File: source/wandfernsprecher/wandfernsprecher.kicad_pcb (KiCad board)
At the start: 2 copper layers, 132.5 x 82 mm, 65 parts, among them J1 Hörer, J2 USB_C_Receptacle_USB2.0, J3 Conn_01x02, Q1 AO3400A, Q10 AO3401A, Q11 AO3400A, Q2 2N5551, Q3 2N5551, Q4 2N5551, Q5 2N5401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

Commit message: completed layout
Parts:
- removed C18: 100n, Capacitor_SMD:C_0603_1608Metric
- removed J2: USB_C_Receptacle_USB2.0, Connector_USB:USB_C_Receptacle_HRO_TYPE-C-31-M-12
- removed R24: 10k, Resistor_SMD:R_0603_1608Metric
- removed R25, R27: 5k1, Resistor_SMD:R_0603_1608Metric
- added BT1: Battery_Cell, Connector_JST:JST_PH_B2B-PH-K_1x02_P2.00mm_Vertical, F.Cu at (90.8, 84.5)
- added C10: 100nF, Capacitor_SMD:C_0603_1608Metric, F.Cu at (84.5, 126.2)
- added C19: 10µF, Capacitor_SMD:C_0603_1608Metric, F.Cu at (86.8, 142.2)
- added C20: 1µF, Capacitor_SMD:C_0603_1608Metric, F.Cu at (86.5, 138.5)
- added C6: 1µF, Capacitor_SMD:C_0603_1608Metric, F.Cu at (95.8, 98.1)
- added C7: 1µF, Capacitor_SMD:C_0603_1608Metric, F.Cu at (93.8, 92.3)
- added C8: 10µF, Capacitor_SMD:C_0603_1608Metric, F.Cu at (82.0, 126.2)
- added C9: 10nF, Capacitor_SMD:C_0603_1608Metric, F.Cu at (79.5, 121.8)
- added D2: GRN, LED_SMD:LED_0805_2012Metric, F.Cu at (81.8, 82.5)
- added D3: YEL, LED_SMD:LED_0805_2012Metric, F.Cu at (84.0, 82.5)
- added D4: 5,1V, Diode_SMD:D_SOD-123, F.Cu at (102.5, 81.0)
- added JP1: SolderJumper_2_Open, Jumper:SolderJumper-2_P1.3mm_Open_RoundedPad1.0x1.5mm, F.Cu at (90.8, 99.2)
- added JP2: SolderJumper_2_Open, Jumper:SolderJumper-2_P1.3mm_Open_RoundedPad1.0x1.5mm, F.Cu at (88.2, 99.2)
- added R28: 1k6, Resistor_SMD:R_0603_1608Metric, F.Cu at (90.2, 96.0)
- added R29: 820, Resistor_SMD:R_0603_1608Metric, F.Cu at (88.8, 96.0)
- added R30: 1k, Resistor_SMD:R_0603_1608Metric, F.Cu at (97.2, 87.8)
- added R31: 10k, Resistor_SMD:R_0603_1608Metric, F.Cu at (95.8, 87.8)
- added R32: 1k6, Resistor_SMD:R_0603_1608Metric, F.Cu at (101.5, 95.0)
- added R33: 1k6, Resistor_SMD:R_0603_1608Metric, F.Cu at (101.5, 93.2)
- added SW3: SW_SPST, Connector_JST:JST_PH_B2B-PH-K_1x02_P2.00mm_Vertical, F.Cu at (100.8, 75.0)
- added U8: TPS73633DBV, Package_TO_SOT_SMD:SOT-23-5, F.Cu at (83.2, 122.8)
- C1, C11, C16, C2, C3, C4, C5: value 100n -> 100nF
- C13, C15: value 1µ -> 1µF
- J1, NS1, SW2: footprint FeWAp:CONN_01x04_vertical -> FeWAp:CONN_01x04_vertical_mod
- J3: value Conn_01x02 -> Conn_01x04; footprint Connector_JST:JST_PH_B2B-PH-K_1x02_P2.00mm_Vertical -> Connector_PinHeader_2.54mm:PinHeader_1x04_P2.54mm_Vertical
- L1: footprint FeWAp:CONN_01x02_vertical -> FeWAp:CONN_01x02_vertical_mod
- U2: footprint Espressif:ESP32-C3-WROOM-02 -> RF_Module:ESP32-C3-WROOM-02
- moved R17 240.2 mm to (124.8, 131.2), turned to -90 degrees
- moved R18 237.3 mm to (124.8, 128.0), turned to -90 degrees
- moved D1 236.4 mm to (121.0, 136.5), turned to 180 degrees
- moved U4 227.8 mm to (115.2, 125.1), turned to -90 degrees
- moved R16 227.8 mm to (112.8, 124.2), turned to -90 degrees
- moved R8 225.0 mm to (100.8, 132.5), turned to 0 degrees
- moved Q1 224.0 mm to (100.8, 135.2)
- moved R10 223.6 mm to (101.8, 138.8), turned to -90 degrees
- moved C13 221.9 mm to (109.5, 124.0), turned to 180 degrees
- moved Q8 221.1 mm to (100.8, 142.2), turned to -90 degrees
- moved R9 220.8 mm to (99.8, 138.8), turned to -90 degrees
- moved C14 217.7 mm to (125.0, 144.2), turned to 180 degrees
- moved L2 217.5 mm to (107.0, 143.0), turned to 0 degrees
- moved C12 216.2 mm to (108.0, 133.6), turned to 90 degrees
- moved Q2 190.9 mm to (131.2, 136.2)
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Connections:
- net Net-(C13-Pad1) renamed /Bells/HV_{C}'
- net Net-(J1-MIC+) renamed /S+
- net Net-(J1-MIC-) renamed /S-
- net Net-(J1-SPK+) renamed /M+
- net Net-(J1-SPK-) renamed /M-
- net Net-(Q1-D) renamed /Bells/~{HV_EN}
- net Net-(Q8-D) renamed /Bells/HV-IN
- net Net-(U4-FB) renamed /Bells/HV-FB
- net Net-(U4-V_{C}) renamed /Bells/HV-C
- C15 pad 1: Net-(Q4-E) -> Net-(Q6-E)
- J3 pad 1: +BATT -> GND
- J3 pad 2: GND -> /plug.D+
- L1 pad 1: Net-(C15-Pad2) -> Net-(Q4-E)
- L1 pad 2: Net-(Q6-E) -> Net-(C15-Pad2)
- U2 pad 10: BELL_B -> nsa
- U2 pad 3: nsa -> BELL_B
- U2 pad 4: nsi -> BELL_A
- U2 pad 6: BELL_A -> nsi
- U3 pad 1: unconnected-(U3-IN-Pad1) -> VBUS
- U3 pad 10: unconnected-(U3-OUT-Pad10) -> +BATT
- U3 pad 11: Net-(U3-VSS-Pad11) -> GND
- U3 pad 2: unconnected-(U3-ISET-Pad2) -> /Power Supply/ISET
- U3 pad 3: Net-(U3-VSS-Pad11) -> GND
- U3 pad 5: unconnected-(U3-~{PG}-Pad5) -> /Power Supply/BQ-~{PG}
- U3 pad 7: unconnected-(U3-ISET2-Pad7) -> /Power Supply/ISET2
- U3 pad 8: unconnected-(U3-~{CHG}-Pad8) -> /Power Supply/BQ-~{CHG}
- U3 pad 9: unconnected-(U3-TS-Pad9) -> /Power Supply/TS
- U5 pad 4: /plug_D- -> /plug.D-
- U5 pad 6: /plug_D+ -> /plug.D+
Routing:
- net +4V: track 0.00 -> 144.3 mm, vias 0 -> 5
- net VBUS: track 0.00 -> 114.1 mm, vias 0 -> 3
- net Net-(SW1-S1c): track 0.00 -> 86.9 mm
- net +48V: track 0.00 -> 63.3 mm
- net /ADC_EN: track 0.00 -> 59.2 mm
- net /ADC: track 0.00 -> 55.8 mm
- net ES1: track 0.00 -> 50.4 mm, vias 0 -> 3
- net Net-(Q2-B): track 3.02 -> 50.7 mm
- net +3.3V: track 0.00 -> 46.5 mm, vias 0 -> 2
- net +BATT: track 0.00 -> 45.0 mm
- net Net-(Q4-E): track 0.00 -> 43.8 mm
- net HV_EN: track 0.00 -> 43.4 mm, vias 0 -> 2
- net nsa: track 0.00 -> 39.4 mm, vias 0 -> 2
- net /IO9: track 0.00 -> 37.4 mm, vias 0 -> 1
- net Net-(Q3-B): track 3.40 -> 40.7 mm
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- added copper zone on F.Cu, net /Bells/HV-IN
- added copper zone on In1.Cu, net GND
- added copper zone on In2.Cu, net GND
- added copper zone on F.Cu, net Net-(D1-A)
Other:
- copper layers 2 -> 4

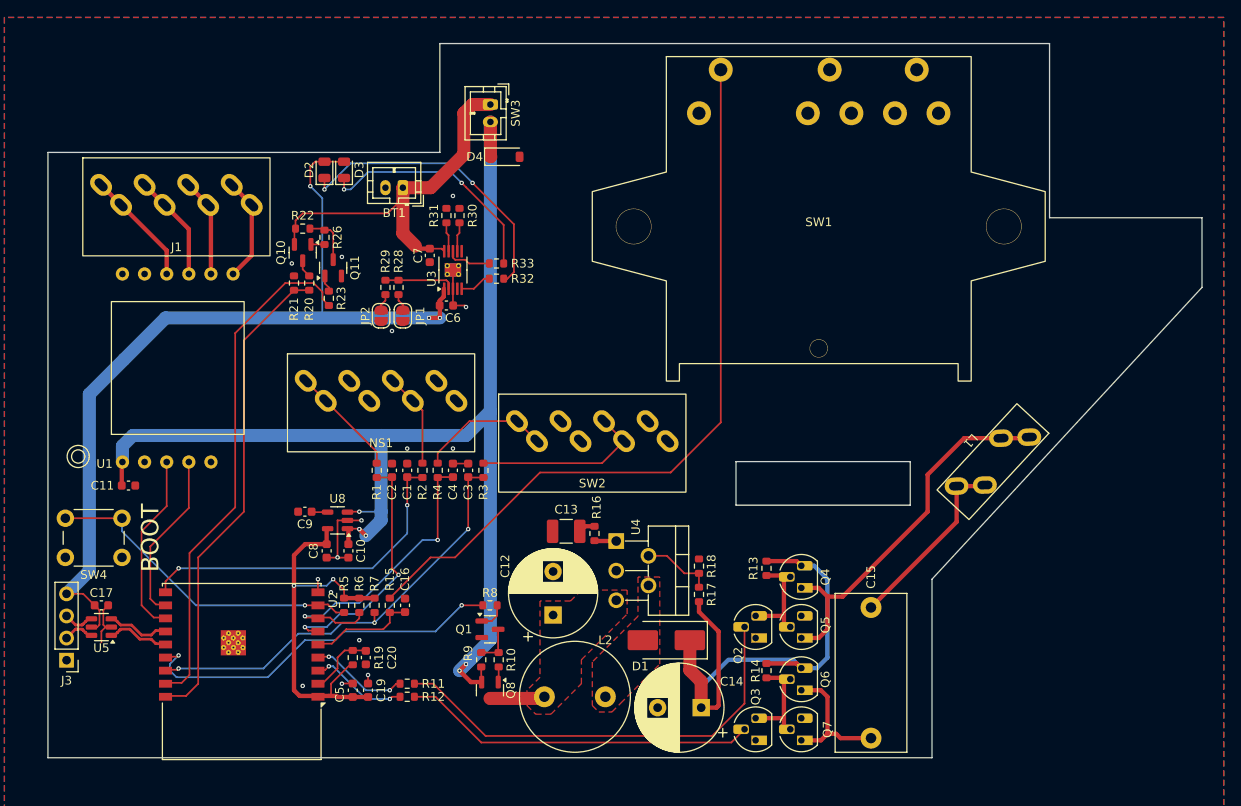
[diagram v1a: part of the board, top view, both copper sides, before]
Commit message: added ibom added switch holder FreeCAD file added Vin header and ideal diodes, finalized layout
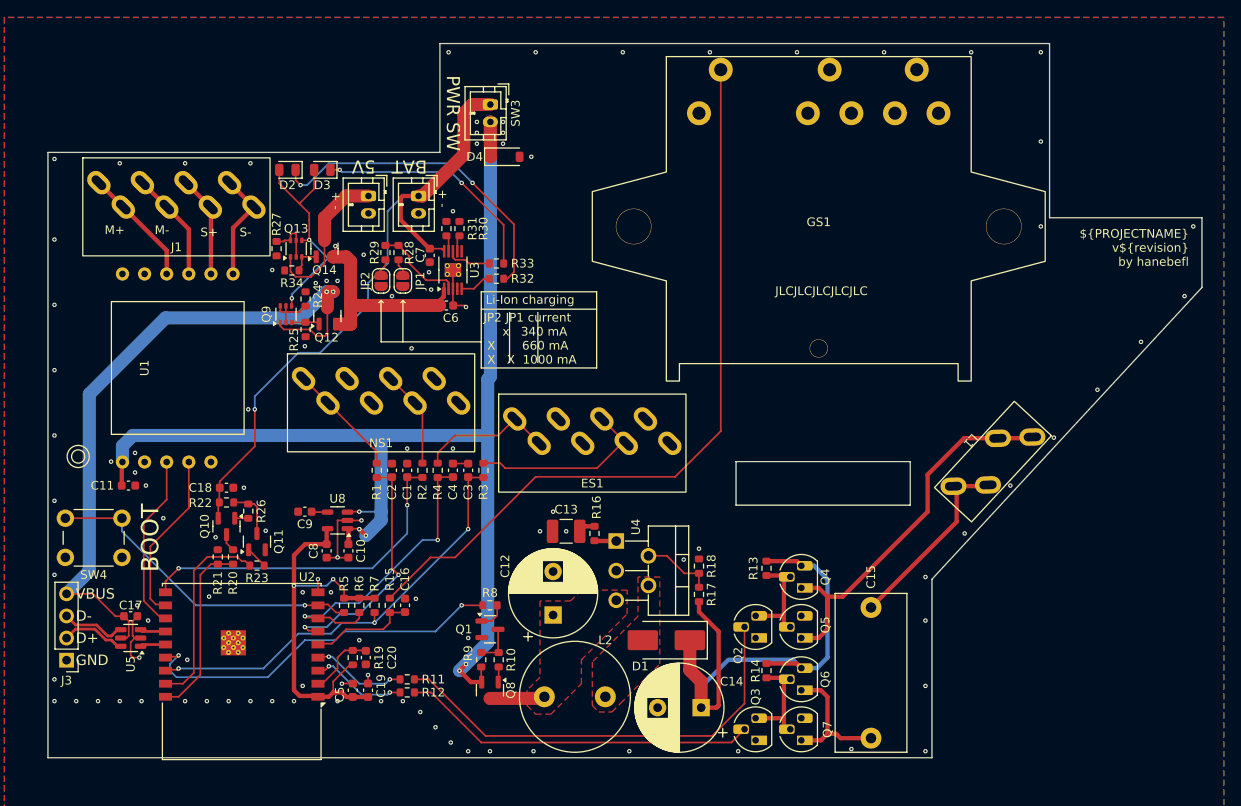
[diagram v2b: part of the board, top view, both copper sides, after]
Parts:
- removed SW1: Gabelschalter, FeWAp:Gabelschalter
- removed SW2: Erdschalter, FeWAp:CONN_01x04_vertical_mod
- added C18: 1µF, Capacitor_SMD:C_0603_1608Metric, F.Cu at (70.5, 119.0)
- added ES1: Erdschalter, FeWAp:CONN_01x04_vertical_mod, F.Cu at (112.5, 112.5)
- added GS1: Gabelschalter, FeWAp:Gabelschalter, F.Cu at (138.5, 89.0)
- added J2: Vin, Connector_JST:JST_PH_B2B-PH-K_1x02_P2.00mm_Vertical, F.Cu at (86.8, 85.5)
- added Q12: AO3401A, Package_TO_SOT_SMD:SOT-23, F.Cu at (82.1, 99.3)
- added Q13: BC857BS, Package_TO_SOT_SMD:SOT-363_SC-70-6, F.Cu at (78.5, 91.5)
- added Q14: AO3401A, Package_TO_SOT_SMD:SOT-23, F.Cu at (81.8, 91.5)
- added Q9: BC857BS, Package_TO_SOT_SMD:SOT-363_SC-70-6, F.Cu at (77.3, 99.1)
- added R24: 10k, Resistor_SMD:R_0603_1608Metric, F.Cu at (79.6, 97.3)
- added R25: 10k, Resistor_SMD:R_0603_1608Metric, F.Cu at (79.6, 100.8)
- added R27: 10k, Resistor_SMD:R_0603_1608Metric, F.Cu at (76.2, 91.5)
- added R34: 10k, Resistor_SMD:R_0603_1608Metric, F.Cu at (78.0, 94.0)
- moved Q10 32.6 mm to (70.5, 123.4)
- moved Q11 32.6 mm to (74.0, 125.2)
- moved R20 32.6 mm to (71.2, 126.9)
- moved R21 32.6 mm to (69.5, 126.9)
- moved R22 32.6 mm to (70.5, 120.7)
- moved R26 32.6 mm to (73.0, 121.7)
- moved R23 31.8 mm to (74.0, 127.9), turned to 180 degrees
- moved D2 4.25 mm to (77.5, 82.5), turned to 180 degrees
- moved JP1 4.00 mm to (90.8, 95.2)
- moved JP2 4.00 mm to (88.2, 95.2)
- moved R28 4.00 mm to (90.2, 92.0)
- moved R29 4.00 mm to (88.8, 92.0)
- moved C17 3.59 mm to (59.5, 133.8)
- moved U5 3.59 mm to (59.5, 136.2)
- moved D3 2.50 mm to (81.5, 82.5), turned to 180 degrees
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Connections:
- C6 pad 1: VBUS -> /Power Supply/Vin'
- D2 pad 2: VBUS -> /Power Supply/Vin'
- D3 pad 2: VBUS -> /Power Supply/Vin'
- U3 pad 1: VBUS -> /Power Supply/Vin'
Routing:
- net /Power Supply/Vin': track 0.00 -> 51.5 mm, vias 0 -> 3
- net /ADC_EN: track 59.2 -> 23.0 mm
- net /ADC: track 55.8 -> 20.8 mm
- net VBUS: track 114.1 -> 79.8 mm, vias 3 -> 2
- net +BATT: track 45.0 -> 75.6 mm, vias 0 -> 1
- net Net-(J2-Pin_1): track 0.00 -> 17.8 mm
- net Net-(Q13A-B1): track 0.00 -> 5.80 mm
- net Net-(Q9A-B1): track 0.00 -> 5.69 mm
- net USB_D-: track 7.21 -> 2.95 mm
- net USB_D+: track 7.21 -> 2.95 mm
- net unconnected-(SW2-NC-Pad4): track 0.00 -> 3.96 mm
- net /plug.D-: track 3.60 -> 7.48 mm
- net /plug.D+: track 3.60 -> 7.48 mm
- net Net-(Q13B-C2): track 0.00 -> 3.44 mm
- net Net-(Q12-G): track 0.00 -> 3.25 mm
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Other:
- board text added: "${PROJECTNAME} v${REVISION} by hanebefl"
- board text added: "+ -"
- board text added: "5V"
- board text added: "BAT"
- board text added: "D+"
- board text added: "D-"
- board text added: "GND"
- board text added: "JLCJLCJLCJLCJLC"
- board text added: "JP2 JP1 current x 340 mA X 660 mA X X 1000 mA"
- board text added: "Li-Ion charging"
- board text added: "M+"
- board text added: "M-"
- board text added: "S+"
- board text added: "S-"
- board text added: "VBUS"
